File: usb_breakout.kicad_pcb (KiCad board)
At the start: 2 copper layers, 89 x 25 mm, 10 parts, among them J1 USB_A, J2 Conn_02x02_Odd_Even, J3 Conn_01x04, J4 Conn_01x04, J5 Conn_02x02_Odd_Even, J8 USB_A

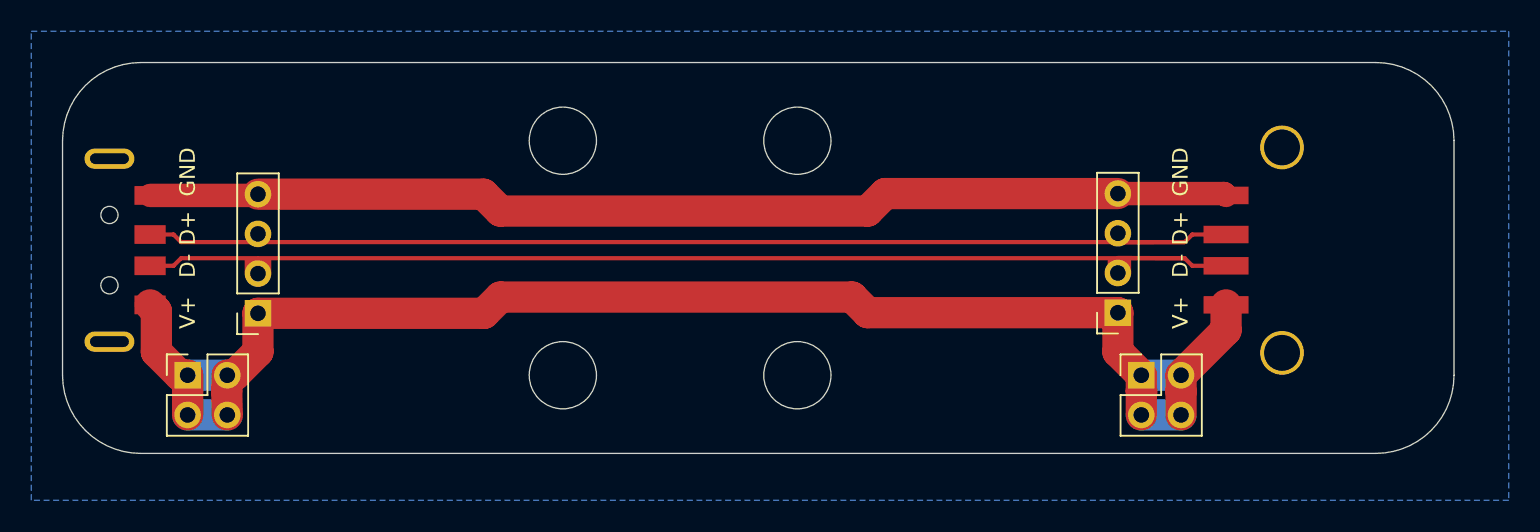
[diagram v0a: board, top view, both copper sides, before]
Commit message: compacting layout
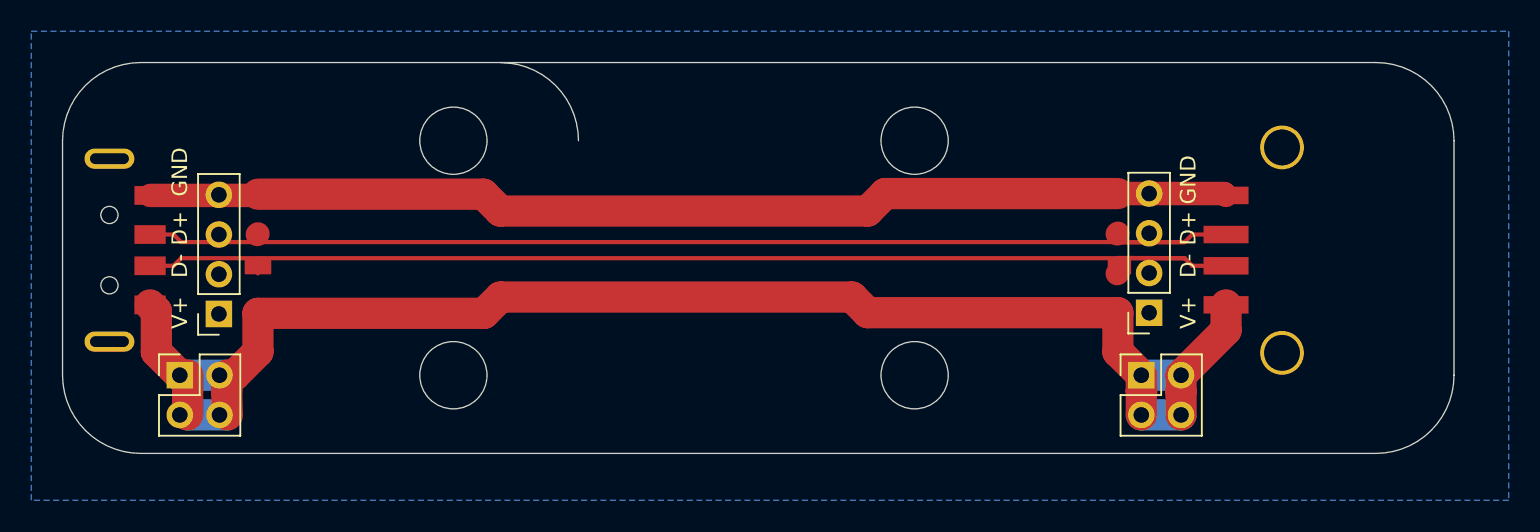
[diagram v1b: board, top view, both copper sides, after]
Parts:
- moved H3 7.50 mm to (169.5, 87.0)
- moved H4 7.50 mm to (169.5, 102.0)
- moved H1 7.00 mm to (140.0, 87.0)
- moved H2 7.00 mm to (140.0, 102.0)
- moved J3 2.50 mm to (125.0, 98.1)
- moved J4 2.00 mm to (184.5, 98.0)
- moved J2 0.50 mm to (122.5, 102.0)
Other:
- outline, holes or cut-outs redrawn

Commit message: added mouse bites, cleaned up board outline * board outline from fusion360 * added 0.5mm hole part for "mouse bites"
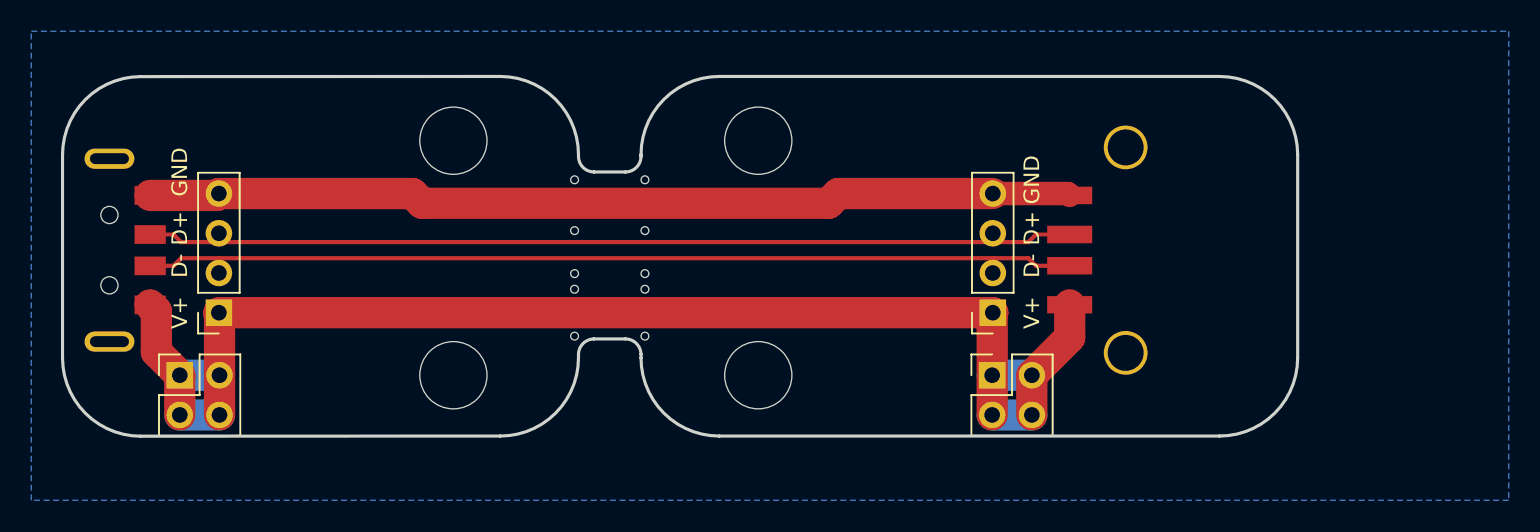
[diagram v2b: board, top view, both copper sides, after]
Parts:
- added REF**: 0.5MM_hole, usb_breakout:0.5MM_hole, F.Cu at (152.2, 99.5)
- added REF**: 0.5MM_hole, usb_breakout:0.5MM_hole, F.Cu at (147.8, 99.5)
- added REF**: 0.5MM_hole, usb_breakout:0.5MM_hole, F.Cu at (152.2, 96.5)
- added REF**: 0.5MM_hole, usb_breakout:0.5MM_hole, F.Cu at (152.2, 95.5)
- added REF**: 0.5MM_hole, usb_breakout:0.5MM_hole, F.Cu at (152.2, 92.8)
- added REF**: 0.5MM_hole, usb_breakout:0.5MM_hole, F.Cu at (152.2, 89.5)
- added REF**: 0.5MM_hole, usb_breakout:0.5MM_hole, F.Cu at (147.8, 89.5)
- added REF**: 0.5MM_hole, usb_breakout:0.5MM_hole, F.Cu at (147.8, 92.8)
- added REF**: 0.5MM_hole, usb_breakout:0.5MM_hole, F.Cu at (147.8, 95.5)
- added REF**: 0.5MM_hole, usb_breakout:0.5MM_hole, F.Cu at (147.8, 96.5)
- moved H3 10.0 mm to (159.5, 87.0)
- moved H4 10.0 mm to (159.5, 102.0)
- moved J4 10.0 mm to (174.5, 98.0)
- moved J8 10.0 mm to (183.0, 94.0)
- moved J5 9.54 mm to (174.5, 102.0)
- moved J3 0.08 mm to (125.0, 98.0)
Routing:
- net /D-: track 75.5 -> 61.1 mm
- net /D+: track 74.7 -> 60.4 mm
- net /GND: track 69.9 -> 59.4 mm
- net /VBUS: track 97.4 -> 88.6 mm
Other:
- board size 89 x 25 mm -> 79 x 23 mm

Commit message: prepare files to be fab'd * create readme with notes * create array * add mouse bites to array * generate gerbers
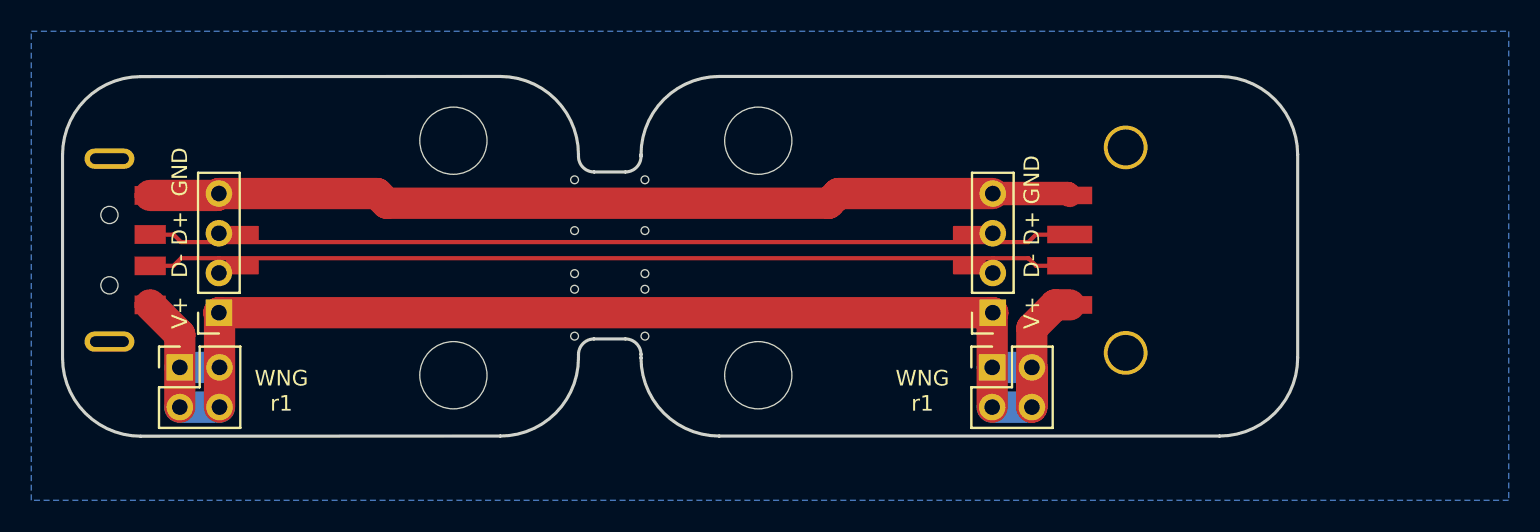
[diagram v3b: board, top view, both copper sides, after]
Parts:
- moved J2 0.50 mm to (122.5, 101.5)
- moved J5 0.50 mm to (174.5, 101.5)
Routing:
- net /VBUS: track 88.6 -> 89.7 mm
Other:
- board text added: "WNG r1"
